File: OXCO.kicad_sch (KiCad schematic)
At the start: 9 parts, among them U4 LT1963AEQ

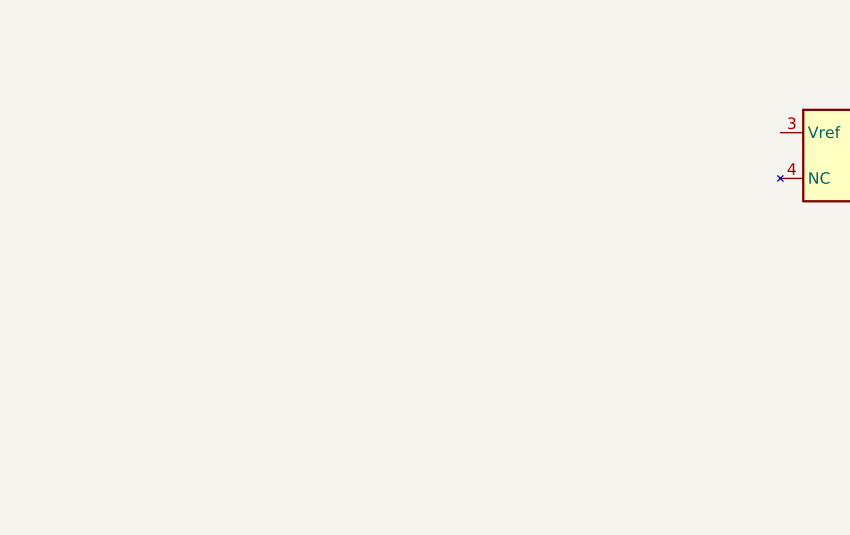
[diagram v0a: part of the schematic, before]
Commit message: OXCO VRef bits
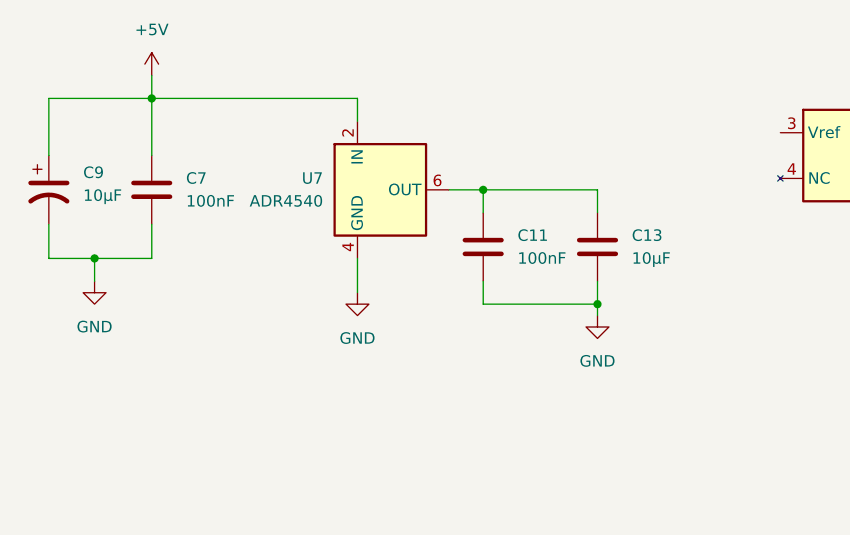
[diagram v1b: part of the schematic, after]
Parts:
- added C11, C7: 100nF, Capacitor_SMD:C_0402_1005Metric_Pad0.74x0.62mm_HandSolder, symbol Device:C
- added C13: 10µF, Capacitor_SMD:C_0805_2012Metric, symbol Device:C
- added C9: 10µF, Capacitor_Tantalum_SMD:CP_EIA-3216-18_Kemet-A, symbol Device:C_Polarized_US
- added U7: ADR4540, Package_SO:SOIC-8_3.9x4.9mm_P1.27mm, symbol Reference_Voltage:ADR4540
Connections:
- net +5V: now also C7.1, C9.1, U7.2 (IN)
- net GND: now also C11.2, C13.2, C7.2, C9.2, U7.4 (GND)
- new net: C11.1, C13.1, U7.6 (OUT)

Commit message: More OXCO circuit work
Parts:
- removed C1: 10u, Capacitor_SMD:C_0805_2012Metric, symbol Device:C
- added C1: 10µF, Capacitor_Tantalum_SMD:CP_EIA-3216-18_Kemet-A, symbol Device:C_Polarized_US
- added C14, C15: 100nF, Capacitor_SMD:C_0402_1005Metric_Pad0.74x0.62mm_HandSolder, symbol Device:C
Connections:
- net GND: now also C1.2
- net LDO_IN: now also C1.1
- net 10MHz: now reaches U5.1 (Out)
- net Vadj: now reaches U5.3 (Vref)
- net Vadj: now also C14.1
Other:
- moved on the sheet: U5

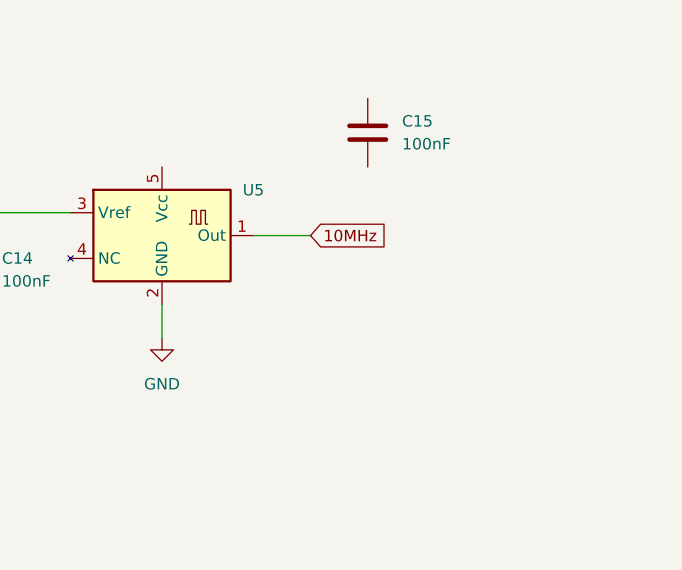
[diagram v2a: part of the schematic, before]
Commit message: More Vadj bits
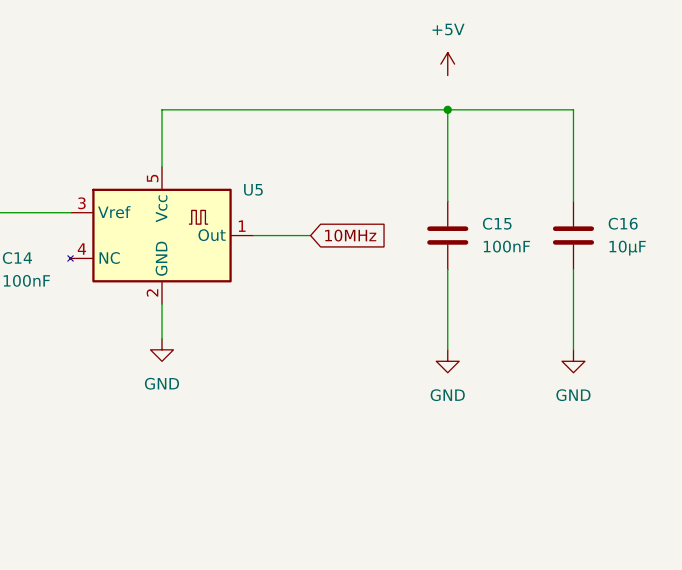
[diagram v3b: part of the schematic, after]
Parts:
- added C16: 10µF, Capacitor_SMD:C_0805_2012Metric, symbol Device:C
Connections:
- net GND: now also C15.2, C16.2
- net at C15.1: now also U5.5 (Vcc), C16.1
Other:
- moved on the sheet: C15
